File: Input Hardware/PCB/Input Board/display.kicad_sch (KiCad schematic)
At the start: 10 parts

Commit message: images and pcb stuff
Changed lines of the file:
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@@
+	(wire
+		(pts
+			(xy 140.97 63.5) (xy 142.24 63.5)
+		)
+		(stroke
+			(width 0)
+			(type default)
+		)
+	)
 	(wire
 		(pts
@@
 	(wire
 		(pts
-			(xy 172.72 73.66) (xy 154.94 73.66)
+			(xy 172.72 73.66) (xy 153.67 73.66)
+		)
+		(stroke
+			(width 0)
+			(type default)
+		)
+	)
+	(wire
+		(pts
+			(xy 163.83 63.5) (xy 162.56 63.5)
 		)
 		(stroke
@@
 	(wire
 		(pts
-			(xy 162.56 71.12) (xy 172.72 71.12)
+			(xy 163.83 71.12) (xy 172.72 71.12)
+		)
+		(stroke
+			(width 0)
+			(type default)
+		)
+	)
+	(wire
+		(pts
+			(xy 153.67 63.5) (xy 154.94 63.5)
 		)
 		(stroke
@@
 	(wire
 		(pts
-			(xy 142.24 78.74) (xy 142.24 63.5)
-		)
-		(stroke
-			(width 0)
-			(type default)
-		)
-	)
-	(wire
-		(pts
-			(xy 149.86 76.2) (xy 172.72 76.2)
+			(xy 140.97 78.74) (xy 140.97 63.5)
+		)
+		(stroke
+			(width 0)
+			(type default)
+		)
+	)
+	(wire
+		(pts
+			(xy 151.13 76.2) (xy 172.72 76.2)
 		)
 		(stroke
@@
 	(wire
 		(pts
-			(xy 172.72 78.74) (xy 142.24 78.74)
+			(xy 172.72 78.74) (xy 140.97 78.74)
 		)
 		(stroke
@@
 	(wire
 		(pts
-			(xy 149.86 63.5) (xy 149.86 76.2)
-		)
-		(stroke
-			(width 0)
-			(type default)
-		)
-	)
-	(wire
-		(pts
-			(xy 154.94 73.66) (xy 154.94 63.5)
+			(xy 151.13 63.5) (xy 151.13 76.2)
+		)
+		(stroke
+			(width 0)
+			(type default)
+		)
+	)
+	(wire
+		(pts
+			(xy 153.67 73.66) (xy 153.67 63.5)
 		)
 		(stroke
@@
 	(wire
 		(pts
-			(xy 162.56 63.5) (xy 162.56 71.12)
+			(xy 163.83 63.5) (xy 163.83 71.12)
 		)
 		(stroke
@@
 		)
 		(stroke
+			(width 0)
+			(type default)
+		)
+	)
+	(wire
+		(pts
+			(xy 151.13 63.5) (xy 149.86 63.5)
+		)
+		(stroke

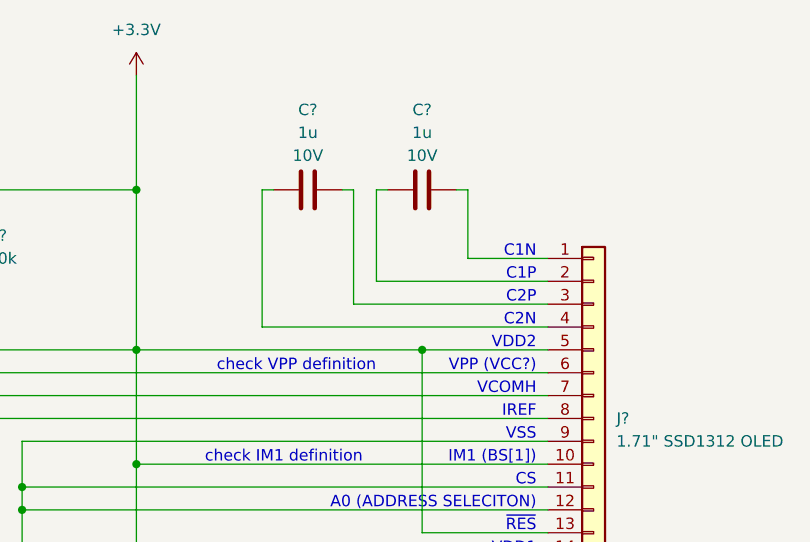
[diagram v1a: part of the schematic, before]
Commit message: Revert "images and pcb stuff"
This reverts commit 6978c7447e140ee759e19aaebffdac22097ec1b9.
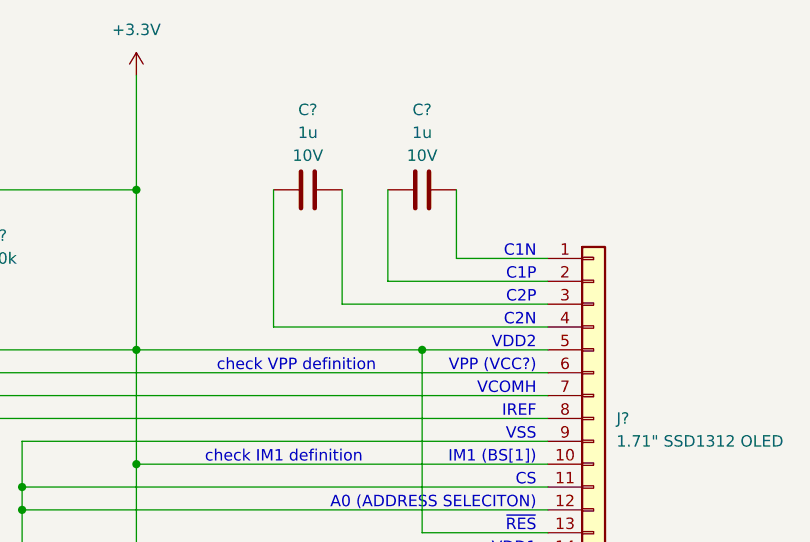
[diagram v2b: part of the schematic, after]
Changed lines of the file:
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@@
-	(wire
-		(pts
-			(xy 140.97 63.5) (xy 142.24 63.5)
-		)
-		(stroke
-			(width 0)
-			(type default)
-		)
-	)
 	(wire
 		(pts
@@
 	(wire
 		(pts
-			(xy 172.72 73.66) (xy 153.67 73.66)
-		)
-		(stroke
-			(width 0)
-			(type default)
-		)
-	)
-	(wire
-		(pts
-			(xy 163.83 63.5) (xy 162.56 63.5)
+			(xy 172.72 73.66) (xy 154.94 73.66)
 		)
 		(stroke
@@
 	(wire
 		(pts
-			(xy 163.83 71.12) (xy 172.72 71.12)
-		)
-		(stroke
-			(width 0)
-			(type default)
-		)
-	)
-	(wire
-		(pts
-			(xy 153.67 63.5) (xy 154.94 63.5)
+			(xy 162.56 71.12) (xy 172.72 71.12)
 		)
 		(stroke
@@
 	(wire
 		(pts
-			(xy 140.97 78.74) (xy 140.97 63.5)
-		)
-		(stroke
-			(width 0)
-			(type default)
-		)
-	)
-	(wire
-		(pts
-			(xy 151.13 76.2) (xy 172.72 76.2)
+			(xy 142.24 78.74) (xy 142.24 63.5)
+		)
+		(stroke
+			(width 0)
+			(type default)
+		)
+	)
+	(wire
+		(pts
+			(xy 149.86 76.2) (xy 172.72 76.2)
 		)
 		(stroke
@@
 	(wire
 		(pts
-			(xy 172.72 78.74) (xy 140.97 78.74)
+			(xy 172.72 78.74) (xy 142.24 78.74)
 		)
 		(stroke
@@
 	(wire
 		(pts
-			(xy 151.13 63.5) (xy 151.13 76.2)
-		)
-		(stroke
-			(width 0)
-			(type default)
-		)
-	)
-	(wire
-		(pts
-			(xy 153.67 73.66) (xy 153.67 63.5)
+			(xy 149.86 63.5) (xy 149.86 76.2)
+		)
+		(stroke
+			(width 0)
+			(type default)
+		)
+	)
+	(wire
+		(pts
+			(xy 154.94 73.66) (xy 154.94 63.5)
 		)
 		(stroke
@@
 	(wire
 		(pts
-			(xy 163.83 63.5) (xy 163.83 71.12)
+			(xy 162.56 63.5) (xy 162.56 71.12)
 		)
 		(stroke
@@
 		)
 		(stroke
-			(width 0)
-			(type default)
-		)
-	)
-	(wire
-		(pts
-			(xy 151.13 63.5) (xy 149.86 63.5)
-		)
-		(stroke

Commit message: kicad fix
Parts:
- removed C? (x4): 1u, Capacitor_SMD:C_0603_1608Metric, symbol Device:C
- removed C? (x2): 2.2u, Capacitor_SMD:C_0603_1608Metric, symbol Device:C
- removed J?: 1.71" SSD1312 OLED, symbol Connector_Generic:Conn_01x16
- removed R? (x2): 10k, Resistor_SMD:R_0603_1608Metric, symbol Device:R
- removed R?: 550k, Resistor_SMD:R_0603_1608Metric, symbol Device:R
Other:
- note removed: "A0 (ADDRESS SELECITON)"
- note removed: "C1N"
- note removed: "C1P"
- note removed: "C2N"
- note removed: "C2P"
- note removed: "CS"
- note removed: "IM1 (BS[1])"
- note removed: "IREF"
- note removed: "SCL"
- note removed: "SI"
- note removed: "VCOMH"
- note removed: "VDD1"
- note removed: "VDD2"
- note removed: "VPP (VCC?)"
- note removed: "VSS"
- note removed: "check IM1 definition"
- note removed: "check VPP definition"
- note removed: "https://www.aliexpress.com/item/1005006387603619.html"
- note removed: "~{RES}"

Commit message: help
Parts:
- added C? (x4): 1u, Capacitor_SMD:C_0603_1608Metric, symbol Device:C
- added C? (x2): 2.2u, Capacitor_SMD:C_0603_1608Metric, symbol Device:C
- added J?: 1.71" SSD1312 OLED, symbol Connector_Generic:Conn_01x16
- added R? (x2): 10k, Resistor_SMD:R_0603_1608Metric, symbol Device:R
- added R?: 550k, Resistor_SMD:R_0603_1608Metric, symbol Device:R
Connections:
- new net: C?.1, J?.4 (Pin_4)
- new net: C?.2, J?.3 (Pin_3)
- new net: C?.1, J?.6 (Pin_6)
- new net: C?.1, J?.7 (Pin_7)
- new net: C?.2, J?.1 (Pin_1)
- new net: C?.1, J?.2 (Pin_2)
- new net: J?.8 (Pin_8), R?.2
- new net +3.3V: C?.1, C?.1, J?.10 (Pin_10), J?.13 (Pin_13), J?.14 (Pin_14), J?.5 (Pin_5), R?.1, R?.1
- new net GND: C?.2, C?.2, C?.2, C?.2, J?.11 (Pin_11), J?.12 (Pin_12), J?.9 (Pin_9), R?.1
- new net OLED_SCL: J?.15 (Pin_15), R?.2
- new net OLED_SDA: J?.16 (Pin_16), R?.2
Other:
- note added: "A0 (ADDRESS SELECITON)"
- note added: "C1N"
- note added: "C1P"
- note added: "C2N"
- note added: "C2P"
- note added: "CS"
- note added: "IM1 (BS[1])"
- note added: "IREF"
- note added: "SCL"
- note added: "SI"
- note added: "VCOMH"
- note added: "VDD1"
- note added: "VDD2"
- note added: "VPP (VCC?)"
- note added: "VSS"
- note added: "check IM1 definition"
- note added: "check VPP definition"
- note added: "https://www.aliexpress.com/item/1005006387603619.html"
- note added: "~{RES}"
